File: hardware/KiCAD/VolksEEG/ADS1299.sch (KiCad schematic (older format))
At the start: 22 parts, among them J5 Conn_02x04_Counter_Clockwise, U9 ADS1299IPAG

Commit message: General schematic cleanup, and assigning some footprints.
Cleaning up the meta-data within KiCAD, and assigning some basic footprints.
Also, cleaning out some footprint references that didn't point anywhere.
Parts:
- R32, R33, R34, R35, R36, R37: footprint (none) -> Resistor_SMD:R_0603_1608Metric_Pad0.98x0.95mm_HandSolder
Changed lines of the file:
@@
 F 0 "R32" H 2120 4696 50  0000 L CNN
 F 1 "10K" H 2120 4605 50  0000 L CNN
-F 2 "" V 1980 4650 50  0001 C CNN
+F 2 "Resistor_SMD:R_0603_1608Metric_Pad0.98x0.95mm_HandSolder" V 1980 4650 50  0001 C CNN
 F 3 "~" H 2050 4650 50  0001 C CNN
 	1    2050 4650
@@
 F 0 "R37" V 6750 2100 50  0000 L CNN
 F 1 "10K" V 6750 1900 50  0000 L CNN
-F 2 "" V 6580 2050 50  0001 C CNN
+F 2 "Resistor_SMD:R_0603_1608Metric_Pad0.98x0.95mm_HandSolder" V 6580 2050 50  0001 C CNN
 F 3 "~" H 6650 2050 50  0001 C CNN
 	1    6650 2050
@@
 F 0 "R36" V 4150 900 50  0000 L CNN
 F 1 "10K" V 4150 1050 50  0000 L CNN
-F 2 "" V 3980 1000 50  0001 C CNN
+F 2 "Resistor_SMD:R_0603_1608Metric_Pad0.98x0.95mm_HandSolder" V 3980 1000 50  0001 C CNN
 F 3 "~" H 4050 1000 50  0001 C CNN
 	1    4050 1000
@@
 F 0 "R35" V 3900 900 50  0000 L CNN
 F 1 "10K" V 3900 1050 50  0000 L CNN
-F 2 "" V 3730 1000 50  0001 C CNN
+F 2 "Resistor_SMD:R_0603_1608Metric_Pad0.98x0.95mm_HandSolder" V 3730 1000 50  0001 C CNN
 F 3 "~" H 3800 1000 50  0001 C CNN
 	1    3800 1000
@@
 F 0 "R34" V 3650 900 50  0000 L CNN
 F 1 "10K" V 3650 1050 50  0000 L CNN
-F 2 "" V 3480 1000 50  0001 C CNN
+F 2 "Resistor_SMD:R_0603_1608Metric_Pad0.98x0.95mm_HandSolder" V 3480 1000 50  0001 C CNN
 F 3 "~" H 3550 1000 50  0001 C CNN
 	1    3550 1000
@@
 F 0 "R33" H 2970 4146 50  0000 L CNN
 F 1 "10K" H 2970 4055 50  0000 L CNN
-F 2 "" V 2830 4100 50  0001 C CNN
+F 2 "Resistor_SMD:R_0603_1608Metric_Pad0.98x0.95mm_HandSolder" V 2830 4100 50  0001 C CNN
 F 3 "~" H 2900 4100 50  0001 C CNN
 	1    2900 4100

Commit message: Change ADS1299 over to using the KiCAD library footprint.
Also deleted the custom drawn QFP footprint.
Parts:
- U9: footprint VolksEEG:QFP50P1200X1200X120-64N -> Package_QFP:LQFP-64_10x10mm_P0.5mm
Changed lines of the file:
@@
 F 0 "U9" H 4850 6620 50  0000 C CNN
 F 1 "ADS1299IPAG" H 4850 6529 50  0000 C CNN
-F 2 "VolksEEG:QFP50P1200X1200X120-64N" H 4850 3850 50  0001 L BNN
+F 2 "Package_QFP:LQFP-64_10x10mm_P0.5mm" H 4850 3850 50  0001 L BNN
 F 3 "http://www.ti.com/lit/ds/symlink/ads1299.pdf" H 4850 3850 50  0001 L BNN
 	1    4850 3850

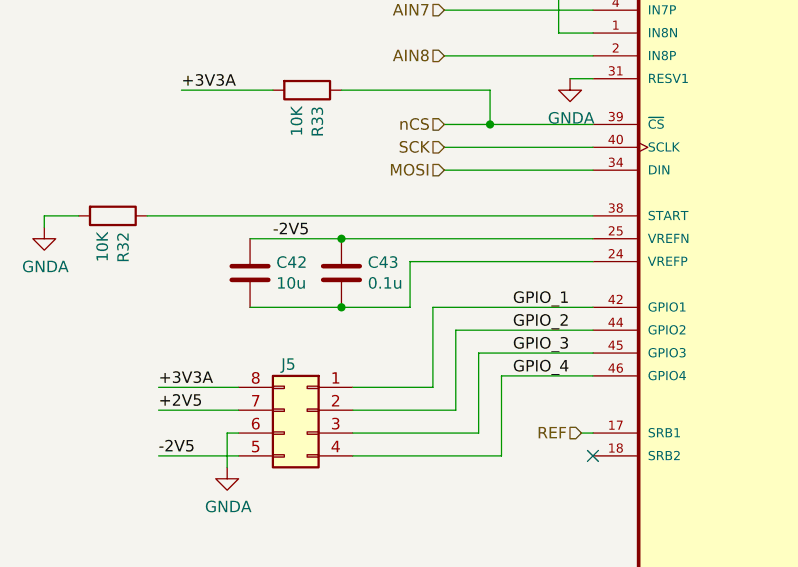
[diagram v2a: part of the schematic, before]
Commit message: Updated some footprints and part manufacturers and numbers.
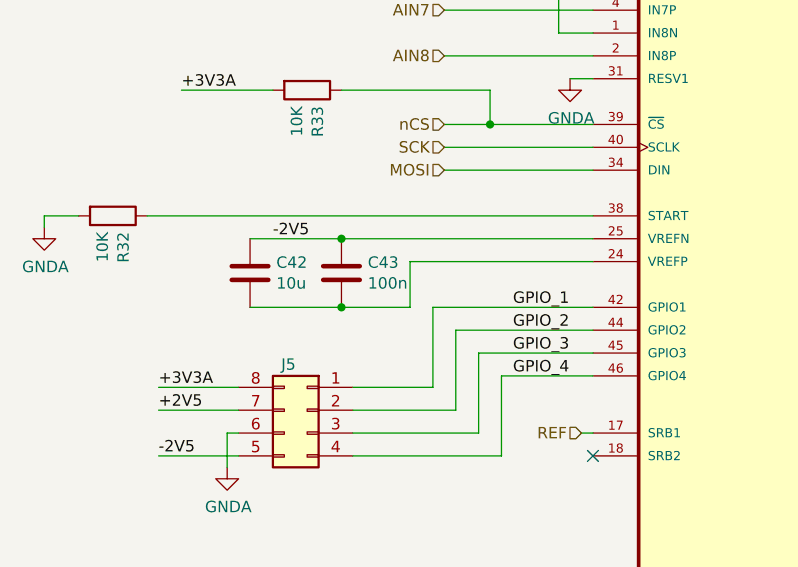
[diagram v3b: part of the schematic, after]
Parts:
- C42: footprint (none) -> Capacitor_SMD:C_0603_1608Metric_Pad1.08x0.95mm_HandSolder; Manufacturer (none) -> Samsung Electro-Mechanics; Part Number (none) -> CL21B106KPQNNNE
- C43: value 0.1u -> 100n; footprint (none) -> Capacitor_SMD:C_0603_1608Metric_Pad1.08x0.95mm_HandSolder; Manufacturer (none) -> Samsung Electro-Mechanics; Part Number (none) -> CL21B104KACNNNC
- C44, C48, C50, C51, C53: footprint (none) -> Capacitor_SMD:C_0603_1608Metric_Pad1.08x0.95mm_HandSolder; Manufacturer (none) -> Samsung Electro-Mechanics; Part Number (none) -> CL21B104KACNNNC
- C45, C46, C47, C49, C52, C54: footprint (none) -> Capacitor_SMD:C_0603_1608Metric_Pad1.08x0.95mm_HandSolder; Manufacturer (none) -> Samsung Electro-Mechanics; Part Number (none) -> CL21B105KAFNNNE
- C55: footprint (none) -> Capacitor_SMD:C_1210_3225Metric_Pad1.33x2.70mm_HandSolder; Manufacturer (none) -> Kyocera AVX; Part Number (none) -> 1210YD107MAT2A
- J5: footprint (none) -> Connector_PinHeader_2.54mm:PinHeader_2x04_P2.54mm_Vertical; Manufacturer (none) -> TE Connectivity AMP Connectors; Part Number (none) -> 5-146256-4
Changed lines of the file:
@@
 	5550 2100 5550 2000
 Connection ~ 5550 2000
-$Comp
-L Device:C C46
-U 1 1 6178451D
-P 6000 5150
-F 0 "C46" H 6115 5196 50  0000 L CNN
-F 1 "1u" H 6115 5105 50  0000 L CNN
-F 2 "" H 6038 5000 50  0001 C CNN
-F 3 "~" H 6000 5150 50  0001 C CNN
-	1    6000 5150
-	1    0    0    -1
-$EndComp
-$Comp
-L Device:C C52
-U 1 1 61785139
-P 6400 5150
-F 0 "C52" H 6515 5196 50  0000 L CNN
-F 1 "1u" H 6515 5105 50  0000 L CNN
-F 2 "" H 6438 5000 50  0001 C CNN
-F 3 "~" H 6400 5150 50  0001 C CNN
-	1    6400 5150
-	1    0    0    -1
-$EndComp
-$Comp
-L Device:C C53
-U 1 1 61785494
-P 6800 5150
-F 0 "C53" H 6915 5196 50  0000 L CNN
-F 1 "100n" H 6915 5105 50  0000 L CNN
-F 2 "" H 6838 5000 50  0001 C CNN
-F 3 "~" H 6800 5150 50  0001 C CNN
-	1    6800 5150
-	1    0    0    -1
-$EndComp
-$Comp
-L Device:C C54
-U 1 1 617858A2
-P 7150 5150
-F 0 "C54" H 7265 5196 50  0000 L CNN
-F 1 "1u" H 7265 5105 50  0000 L CNN
-F 2 "" H 7188 5000 50  0001 C CNN
-F 3 "~" H 7150 5150 50  0001 C CNN
-	1    7150 5150
-	1    0    0    -1
-$EndComp
-Wire Wire Line
-	5550 5000 6000 5000
 Wire Wire Line
 	5550 4800 7150 4800
 Wire Wire Line
-	7150 4800 7150 5000
-Wire Wire Line
-	6800 5000 6800 4900
-Wire Wire Line
-	6800 4900 6400 4900
-Wire Wire Line
-	6400 5000 6400 4900
-Connection ~ 6400 4900
-Wire Wire Line
-	6400 4900 5550 4900
-Wire Wire Line
 	5550 4700 7500 4700
-Wire Wire Line
-	7500 4700 7500 5000
-$Comp
-L Device:C C55
-U 1 1 6179D4A4
-P 7500 5150
-F 0 "C55" H 7615 5196 50  0000 L CNN
-F 1 "100u" H 7615 5105 50  0000 L CNN
-F 2 "" H 7538 5000 50  0001 C CNN
-F 3 "~" H 7500 5150 50  0001 C CNN
-	1    7500 5150
-	1    0    0    -1
-$EndComp
 Wire Wire Line
 	5550 2550 5700 2550
@@
 F 0 "C50" V 6200 2100 50  0000 L CNN
 F 1 "100n" V 6200 1850 50  0000 L CNN
-F 2 "" H 6088 1850 50  0001 C CNN
+F 2 "Capacitor_SMD:C_0603_1608Metric_Pad1.08x0.95mm_HandSolder" H 6088 1850 50  0001 C CNN
 F 3 "~" H 6050 2000 50  0001 C CNN
+F 4 "Samsung Electro-Mechanics" H 6050 2000 50  0001 C CNN "Manufacturer"
+F 5 "CL21B104KACNNNC" H 6050 2000 50  0001 C CNN "Part Number"
 	1    6050 2000
 	0    1    1    0
@@
 F 0 "C49" V 6200 1600 50  0000 L CNN
 F 1 "1u" V 6200 1750 50  0000 L CNN
-F 2 "" H 6088 1650 50  0001 C CNN
+F 2 "Capacitor_SMD:C_0603_1608Metric_Pad1.08x0.95mm_HandSolder" H 6088 1650 50  0001 C CNN
 F 3 "~" H 6050 1800 50  0001 C CNN
+F 4 "Samsung Electro-Mechanics" H 6050 1800 50  0001 C CNN "Manufacturer"
+F 5 "CL21B105KAFNNNE" H 6050 1800 50  0001 C CNN "Part Number"
 	1    6050 1800
 	0    -1   -1   0
@@
 F 0 "C48" V 6200 1450 50  0000 L CNN
 F 1 "100n" V 6200 1200 50  0000 L CNN
-F 2 "" H 6088 1200 50  0001 C CNN
+F 2 "Capacitor_SMD:C_0603_1608Metric_Pad1.08x0.95mm_HandSolder" H 6088 1200 50  0001 C CNN
 F 3 "~" H 6050 1350 50  0001 C CNN
+F 4 "Samsung Electro-Mechanics" H 6050 1350 50  0001 C CNN "Manufacturer"
+F 5 "CL21B104KACNNNC" H 6050 1350 50  0001 C CNN "Part Number"
 	1    6050 1350
 	0    1    1    0
@@
 F 0 "C47" V 5900 1250 50  0000 L CNN
 F 1 "1u" V 5900 1100 50  0000 L CNN
-F 2 "" H 6088 1000 50  0001 C CNN
+F 2 "Capacitor_SMD:C_0603_1608Metric_Pad1.08x0.95mm_HandSolder" H 6088 1000 50  0001 C CNN
 F 3 "~" H 6050 1150 50  0001 C CNN
+F 4 "Samsung Electro-Mechanics" H 6050 1150 50  0001 C CNN "Manufacturer"
+F 5 "CL21B105KAFNNNE" H 6050 1150 50  0001 C CNN "Part Number"
 	1    6050 1150
 	0    1    1    0
@@
 F 0 "C45" H 5915 6246 50  0000 L CNN
 F 1 "1u" H 5915 6155 50  0000 L CNN
-F 2 "" H 5838 6050 50  0001 C CNN
+F 2 "Capacitor_SMD:C_0603_1608Metric_Pad1.08x0.95mm_HandSolder" H 5838 6050 50  0001 C CNN
 F 3 "~" H 5800 6200 50  0001 C CNN
+F 4 "Samsung Electro-Mechanics" H 5800 6200 50  0001 C CNN "Manufacturer"
+F 5 "CL21B105KAFNNNE" H 5800 6200 50  0001 C CNN "Part Number"
 	1    5800 6200
 	1    0    0    -1
@@
 P 3050 4900
 F 0 "C43" H 3165 4946 50  0000 L CNN
-F 1 "0.1u" H 3165 4855 50  0000 L CNN
-F 2 "" H 3088 4750 50  0001 C CNN
+F 1 "100n" H 3165 4855 50  0000 L CNN
+F 2 "Capacitor_SMD:C_0603_1608Metric_Pad1.08x0.95mm_HandSolder" H 3088 4750 50  0001 C CNN
 F 3 "~" H 3050 4900 50  0001 C CNN
+F 4 "Samsung Electro-Mechanics" H 3050 4900 50  0001 C CNN "Manufacturer"
+F 5 "CL21B104KACNNNC" H 3050 4900 50  0001 C CNN "Part Number"
 	1    3050 4900
 	1    0    0    -1
@@
 F 0 "C42" H 2765 4946 50  0000 L CNN
 F 1 "10u" H 2765 4855 50  0000 L CNN
-F 2 "" H 2688 4750 50  0001 C CNN
+F 2 "Capacitor_SMD:C_0603_1608Metric_Pad1.08x0.95mm_HandSolder" H 2688 4750 50  0001 C CNN
 F 3 "~" H 2650 4900 50  0001 C CNN
+F 4 "Samsung Electro-Mechanics" H 2650 4900 50  0001 C CNN "Manufacturer"
+F 5 "CL21B106KPQNNNE" H 2650 4900 50  0001 C CNN "Part Number"
 	1    2650 4900
 	1    0    0    -1
@@
 F 0 "C51" H 6265 6246 50  0000 L CNN
 F 1 "100n" H 6265 6155 50  0000 L CNN
-F 2 "" H 6188 6050 50  0001 C CNN
+F 2 "Capacitor_SMD:C_0603_1608Metric_Pad1.08x0.95mm_HandSolder" H 6188 6050 50  0001 C CNN
 F 3 "~" H 6150 6200 50  0001 C CNN
+F 4 "Samsung Electro-Mechanics" H 6150 6200 50  0001 C CNN "Manufacturer"
+F 5 "CL21B104KACNNNC" H 6150 6200 50  0001 C CNN "Part Number"
 	1    6150 6200
 	1    0    0    -1
@@
 F 0 "C44" H 3700 1600 50  0000 L CNN
 F 1 "100n" H 3700 1700 50  0000 L CNN
-F 2 "" H 3588 1500 50  0001 C CNN
+F 2 "Capacitor_SMD:C_0603_1608Metric_Pad1.08x0.95mm_HandSolder" H 3588 1500 50  0001 C CNN
 F 3 "~" H 3550 1650 50  0001 C CNN
+F 4 "Samsung Electro-Mechanics" H 3550 1650 50  0001 C CNN "Manufacturer"
+F 5 "CL21B104KACNNNC" H 3550 1650 50  0001 C CNN "Part Number"
 	1    3550 1650
 	-1   0    0    1
@@
 Text Label 6500 5450 0    50   ~ 0
 -2V5
-Wire Wire Line
-	6000 5300 6000 5450
-Wire Wire Line
-	6400 5300 6400 5450
 Connection ~ 6400 5450
 Wire Wire Line
 	6400 5450 6000 5450
-Wire Wire Line
-	7500 5300 7500 5450
-Wire Wire Line
-	7150 5300 7150 5450
-Connection ~ 7150 5450
-Wire Wire Line
-	7150 5450 7500 5450
-Wire Wire Line
-	6800 5300 6800 5450
-Wire Wire Line
-	6400 5450 6800 5450
-Wire Wire Line
-	6800 5450 7150 5450
-Connection ~ 6800 5450
 Text Label 3800 5350 0    50   ~ 0
 GPIO_4
@@
 F 0 "J5" H 2950 5700 50  0000 L CNN
 F 1 "Conn_02x04_Counter_Clockwise" H 2995 5680 50  0001 L CNN
-F 2 "" H 2900 5500 50  0001 C CNN
+F 2 "Connector_PinHeader_2.54mm:PinHeader_2x04_P2.54mm_Vertical" H 2900 5500 50  0001 C CNN
 F 3 "~" H 2900 5500 50  0001 C CNN
+F 4 "TE Connectivity AMP Connectors" H 2900 5500 50  0001 C CNN "Manufacturer"
+F 5 "5-146256-4" H 2900 5500 50  0001 C CNN "Part Number"
 	1    2900 5500
 	-1   0    0    -1
@@
 Wire Wire Line
 	3100 5700 3750 5700
+Connection ~ 6800 5450
+Wire Wire Line
+	6400 5450 6800 5450
+Wire Wire Line
+	6800 5450 7150 5450
+Wire Wire Line
+	7150 5450 7500 5450
+Connection ~ 7150 5450
+Connection ~ 6400 4900
+Wire Wire Line
+	6400 4900 5550 4900
+Wire Wire Line
+	6800 4900 6400 4900
+Wire Wire Line
+	6800 5300 6800 5450
+Wire Wire Line
+	7150 5300 7150 5450
+Wire Wire Line
+	7500 5300 7500 5450
+Wire Wire Line
+	6400 5300 6400 5450
+Wire Wire Line
+	6000 5300 6000 5450
+$Comp
+L Device:C C55
+U 1 1 6179D4A4
+P 7500 5150
+F 0 "C55" H 7615 5196 50  0000 L CNN
+F 1 "100u" H 7615 5105 50  0000 L CNN
+F 2 "Capacitor_SMD:C_1210_3225Metric_Pad1.33x2.70mm_HandSolder" H 7538 5000 50  0001 C CNN
+F 3 "~" H 7500 5150 50  0001 C CNN
+F 4 "Kyocera AVX" H 7500 5150 50  0001 C CNN "Manufacturer"
+F 5 "1210YD107MAT2A" H 7500 5150 50  0001 C CNN "Part Number"
+	1    7500 5150
+	1    0    0    -1
+$EndComp
+Wire Wire Line
+	7500 4700 7500 5000
+Wire Wire Line
+	6400 5000 6400 4900
+Wire Wire Line
+	6800 5000 6800 4900
+Wire Wire Line
+	7150 4800 7150 5000
+Wire Wire Line
+	5550 5000 6000 5000
+$Comp
+L Device:C C54
+U 1 1 617858A2
+P 7150 5150
+F 0 "C54" H 7265 5196 50  0000 L CNN
+F 1 "1u" H 7265 5105 50  0000 L CNN
+F 2 "Capacitor_SMD:C_0603_1608Metric_Pad1.08x0.95mm_HandSolder" H 7188 5000 50  0001 C CNN
+F 3 "~" H 7150 5150 50  0001 C CNN
+F 4 "Samsung Electro-Mechanics" H 7150 5150 50  0001 C CNN "Manufacturer"
+F 5 "CL21B105KAFNNNE" H 7150 5150 50  0001 C CNN "Part Number"
+	1    7150 5150
+	1    0    0    -1
+$EndComp
+$Comp
+L Device:C C53
+U 1 1 61785494
+P 6800 5150
+F 0 "C53" H 6915 5196 50  0000 L CNN
+F 1 "100n" H 6915 5105 50  0000 L CNN
+F 2 "Capacitor_SMD:C_0603_1608Metric_Pad1.08x0.95mm_HandSolder" H 6838 5000 50  0001 C CNN
+F 3 "~" H 6800 5150 50  0001 C CNN
+F 4 "Samsung Electro-Mechanics" H 6800 5150 50  0001 C CNN "Manufacturer"
+F 5 "CL21B104KACNNNC" H 6800 5150 50  0001 C CNN "Part Number"
+	1    6800 5150
+	1    0    0    -1
+$EndComp
+$Comp
+L Device:C C52
+U 1 1 61785139
+P 6400 5150
+F 0 "C52" H 6515 5196 50  0000 L CNN
+F 1 "1u" H 6515 5105 50  0000 L CNN
+F 2 "Capacitor_SMD:C_0603_1608Metric_Pad1.08x0.95mm_HandSolder" H 6438 5000 50  0001 C CNN
+F 3 "~" H 6400 5150 50  0001 C CNN
+F 4 "Samsung Electro-Mechanics" H 6400 5150 50  0001 C CNN "Manufacturer"
+F 5 "CL21B105KAFNNNE" H 6400 5150 50  0001 C CNN "Part Number"
+	1    6400 5150
+	1    0    0    -1
+$EndComp
+$Comp
+L Device:C C46
+U 1 1 6178451D
+P 6000 5150
+F 0 "C46" H 6115 5196 50  0000 L CNN
+F 1 "1u" H 6115 5105 50  0000 L CNN
+F 2 "Capacitor_SMD:C_0603_1608Metric_Pad1.08x0.95mm_HandSolder" H 6038 5000 50  0001 C CNN
+F 3 "~" H 6000 5150 50  0001 C CNN
+F 4 "Samsung Electro-Mechanics" H 6000 5150 50  0001 C CNN "Manufacturer"
+F 5 "CL21B105KAFNNNE" H 6000 5150 50  0001 C CNN "Part Number"
+	1    6000 5150
+	1    0    0    -1
+$EndComp
 $EndSCHEMATC

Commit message: Finished adding footprints, and started laying out the isolation section.
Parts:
- R32, R33, R34, R35, R36, R37: Manufacturer (none) -> Stackpole Electronics Inc; Part Number (none) -> RMCF0603JT10K0
- U9: Manufacturer (none) -> Texas Instruments; Part Number (none) -> ADS1299IPAG
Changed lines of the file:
@@
 F 2 "Package_QFP:LQFP-64_10x10mm_P0.5mm" H 4850 3850 50  0001 L BNN
 F 3 "http://www.ti.com/lit/ds/symlink/ads1299.pdf" H 4850 3850 50  0001 L BNN
+F 4 "Texas Instruments" H 4850 3850 50  0001 C CNN "Manufacturer"
+F 5 "ADS1299IPAG" H 4850 3850 50  0001 C CNN "Part Number"
 	1    4850 3850
 	1    0    0    -1
@@
 F 2 "Resistor_SMD:R_0603_1608Metric_Pad0.98x0.95mm_HandSolder" V 1980 4650 50  0001 C CNN
 F 3 "~" H 2050 4650 50  0001 C CNN
+F 4 "Stackpole Electronics Inc" H 2050 4650 50  0001 C CNN "Manufacturer"
+F 5 "RMCF0603JT10K0" H 2050 4650 50  0001 C CNN "Part Number"
 	1    2050 4650
 	0    1    1    0
@@
 F 2 "Resistor_SMD:R_0603_1608Metric_Pad0.98x0.95mm_HandSolder" V 6580 2050 50  0001 C CNN
 F 3 "~" H 6650 2050 50  0001 C CNN
+F 4 "Stackpole Electronics Inc" H 6650 2050 50  0001 C CNN "Manufacturer"
+F 5 "RMCF0603JT10K0" H 6650 2050 50  0001 C CNN "Part Number"
 	1    6650 2050
 	-1   0    0    1
@@
 F 2 "Resistor_SMD:R_0603_1608Metric_Pad0.98x0.95mm_HandSolder" V 3980 1000 50  0001 C CNN
 F 3 "~" H 4050 1000 50  0001 C CNN
+F 4 "Stackpole Electronics Inc" H 4050 1000 50  0001 C CNN "Manufacturer"
+F 5 "RMCF0603JT10K0" H 4050 1000 50  0001 C CNN "Part Number"
 	1    4050 1000
 	-1   0    0    1
@@
 F 2 "Resistor_SMD:R_0603_1608Metric_Pad0.98x0.95mm_HandSolder" V 3730 1000 50  0001 C CNN
 F 3 "~" H 3800 1000 50  0001 C CNN
+F 4 "Stackpole Electronics Inc" H 3800 1000 50  0001 C CNN "Manufacturer"
+F 5 "RMCF0603JT10K0" H 3800 1000 50  0001 C CNN "Part Number"
 	1    3800 1000
 	-1   0    0    1
@@
 F 2 "Resistor_SMD:R_0603_1608Metric_Pad0.98x0.95mm_HandSolder" V 3480 1000 50  0001 C CNN
 F 3 "~" H 3550 1000 50  0001 C CNN
+F 4 "Stackpole Electronics Inc" H 3550 1000 50  0001 C CNN "Manufacturer"
+F 5 "RMCF0603JT10K0" H 3550 1000 50  0001 C CNN "Part Number"
 	1    3550 1000
 	-1   0    0    1
@@
 F 2 "Resistor_SMD:R_0603_1608Metric_Pad0.98x0.95mm_HandSolder" V 2830 4100 50  0001 C CNN
 F 3 "~" H 2900 4100 50  0001 C CNN
+F 4 "Stackpole Electronics Inc" H 2900 4100 50  0001 C CNN "Manufacturer"
+F 5 "RMCF0603JT10K0" H 2900 4100 50  0001 C CNN "Part Number"
 	1    2900 4100
 	0    1    1    0

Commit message: Further PCB Layout.
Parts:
- C55: Manufacturer Kyocera AVX -> Taiyo Yuden; Part Number 1210YD107MAT2A -> LMK325ABJ107MMHP
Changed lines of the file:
@@
 F 2 "Capacitor_SMD:C_1210_3225Metric_Pad1.33x2.70mm_HandSolder" H 7538 5000 50  0001 C CNN
 F 3 "~" H 7500 5150 50  0001 C CNN
-F 4 "Kyocera AVX" H 7500 5150 50  0001 C CNN "Manufacturer"
-F 5 "1210YD107MAT2A" H 7500 5150 50  0001 C CNN "Part Number"
+F 4 "Taiyo Yuden" H 7500 5150 50  0001 C CNN "Manufacturer"
+F 5 "LMK325ABJ107MMHP" H 7500 5150 50  0001 C CNN "Part Number"
 	1    7500 5150
 	1    0    0    -1
